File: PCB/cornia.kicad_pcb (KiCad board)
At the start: 2 copper layers, 159.3 x 104.6 mm, 78 parts, among them J1 Conn_01x01_Pin, SW1 SW_Push, SW10 SW_Push, SW11 SW_Push, SW12 SW_Push, SW13 SW_Push, SW14 SW_Push, SW15 SW_Push, SW16 SW_Push, SW17 SW_Push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

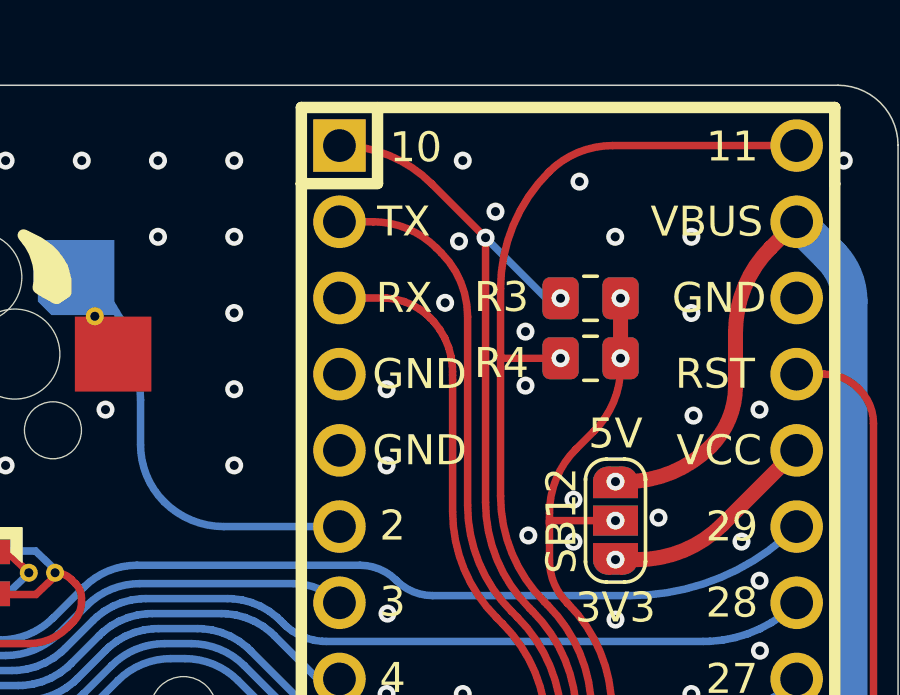
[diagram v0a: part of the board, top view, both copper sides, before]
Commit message: [PCB] Swap TX RX pins
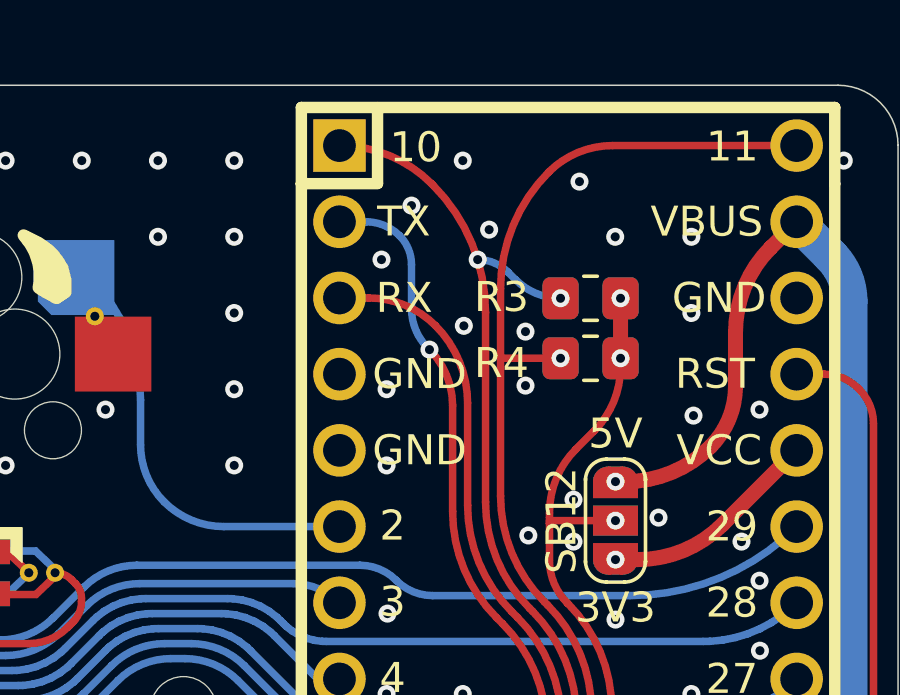
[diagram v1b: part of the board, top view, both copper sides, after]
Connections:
- SB1 pad 1: /TX -> /RX
- SB2 pad 1: /RX_LED -> /TX_LED
- SB3 pad 1: /RX_LED -> /TX_LED
- U1 pad 2: /TX -> /TX_LED
- U1 pad 3: /RX_LED -> /RX
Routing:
- net /TX_LED: track 0.00 -> 52.3 mm, vias 0 -> 1
- net /RX_LED: track 50.4 -> 0.00 mm
- net /TX: track 48.1 -> 0.00 mm
- net /RX: track 0.00 -> 45.5 mm
- net /SDA: track 49.3 -> 48.8 mm
- net GND: vias 445 -> 446

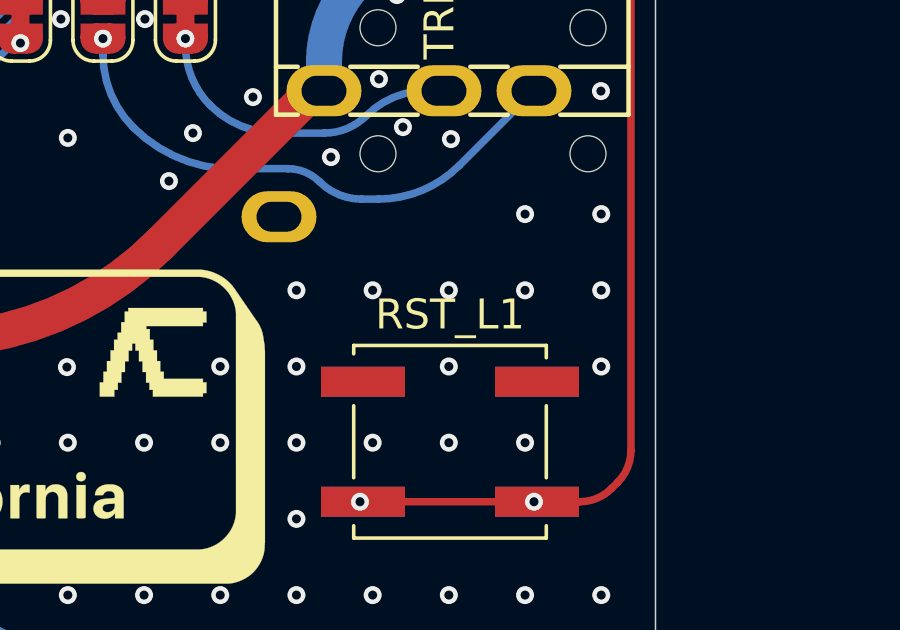
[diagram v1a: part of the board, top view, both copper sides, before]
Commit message: [PCB] Swap RST_L1 & RST_R1 to match their respective sides
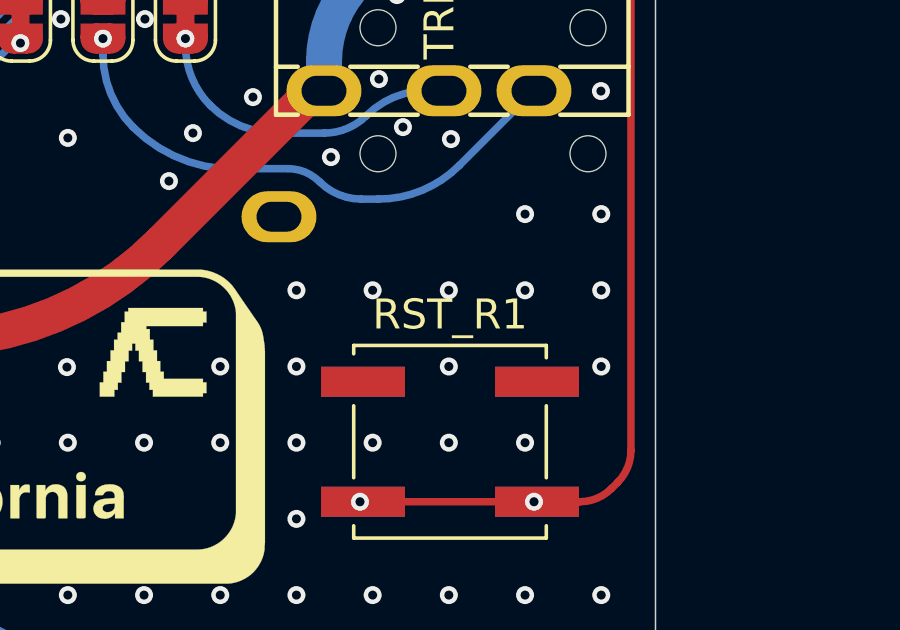
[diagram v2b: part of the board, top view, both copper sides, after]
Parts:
- RST_L1: moved to B.Cu
- RST_R1: moved to F.Cu
- turned RST_L1 to 0 degrees
- turned RST_R1 to 180 degrees

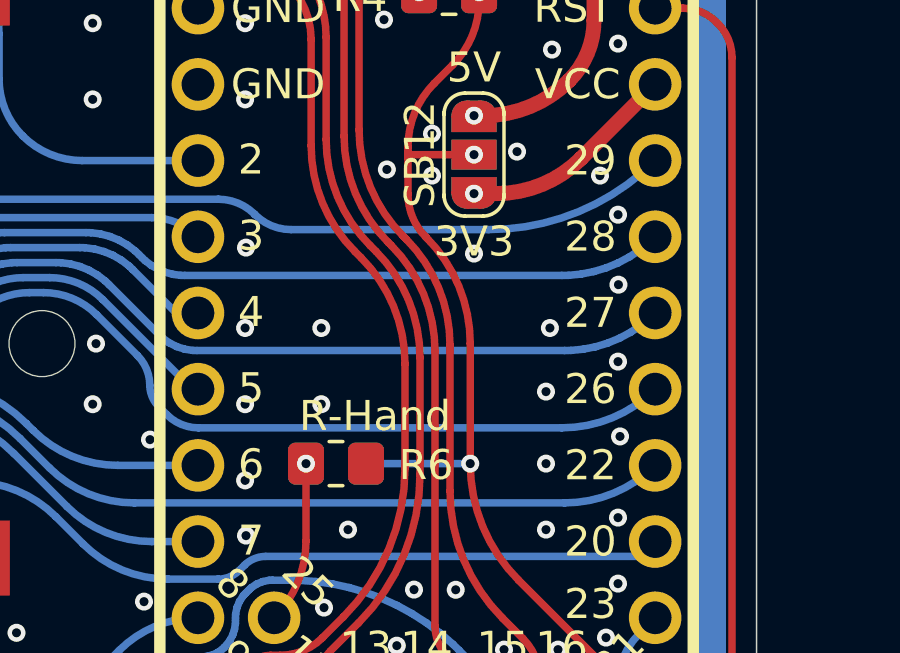
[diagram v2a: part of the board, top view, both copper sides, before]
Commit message: [PCB] Fix handedness pin voltage (fixed to 3v3)
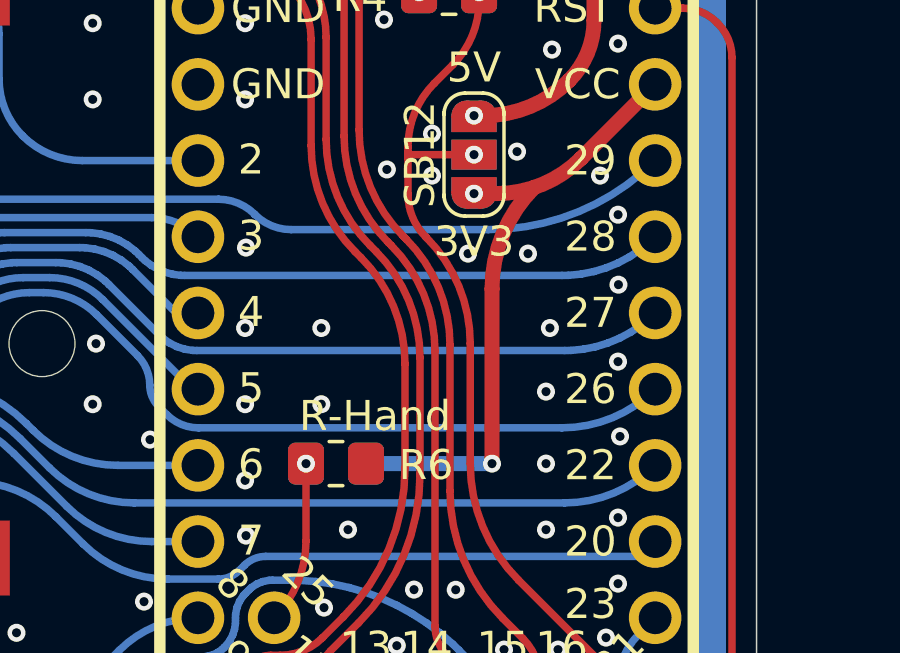
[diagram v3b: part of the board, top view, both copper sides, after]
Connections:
- R5 pad 1: VI2C -> VCC
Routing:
- net VCC: track 7.35 -> 21.1 mm, vias 1 -> 2
- net VI2C: track 44.7 -> 41.3 mm, vias 6 -> 5
- net GND: vias 446 -> 447
